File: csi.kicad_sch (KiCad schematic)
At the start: 90 parts, among them J701 WE_68715014522, J702 WE_68715014522, Q701 BSS138W-7-F, Q702 BSS138W-7-F, Q703 BSS138W-7-F, Q704 BSS138W-7-F, U701 PCA9547BS, U702 AP22615, U703 AP22615, U704 NX3DV642, U705 NX3DV642, U706 AP22615, U707 AP22615

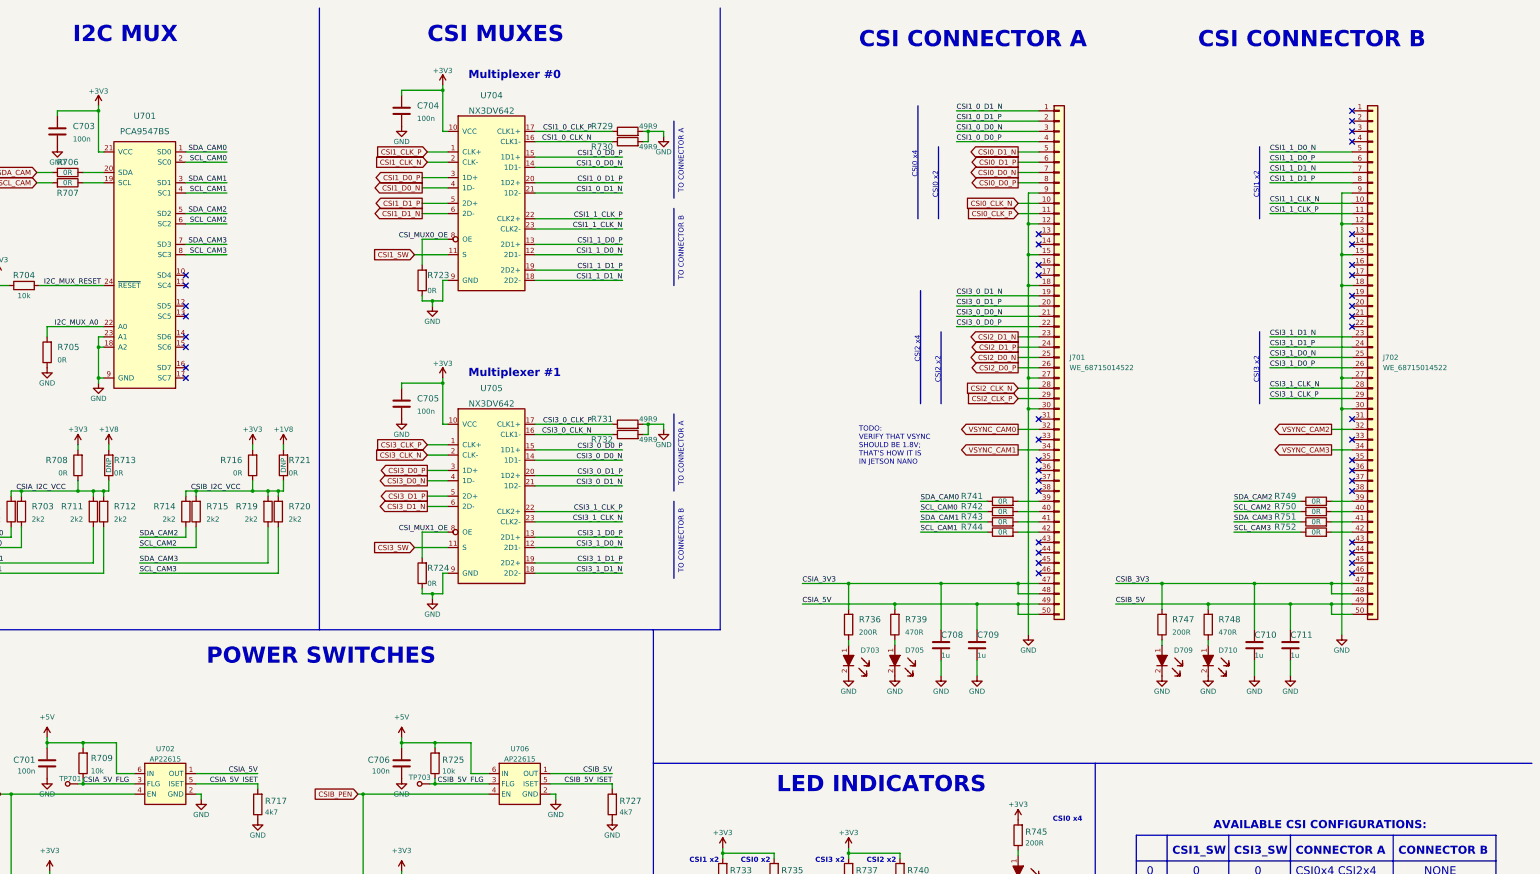
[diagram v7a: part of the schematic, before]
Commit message: Cleaned up schematic after project changes
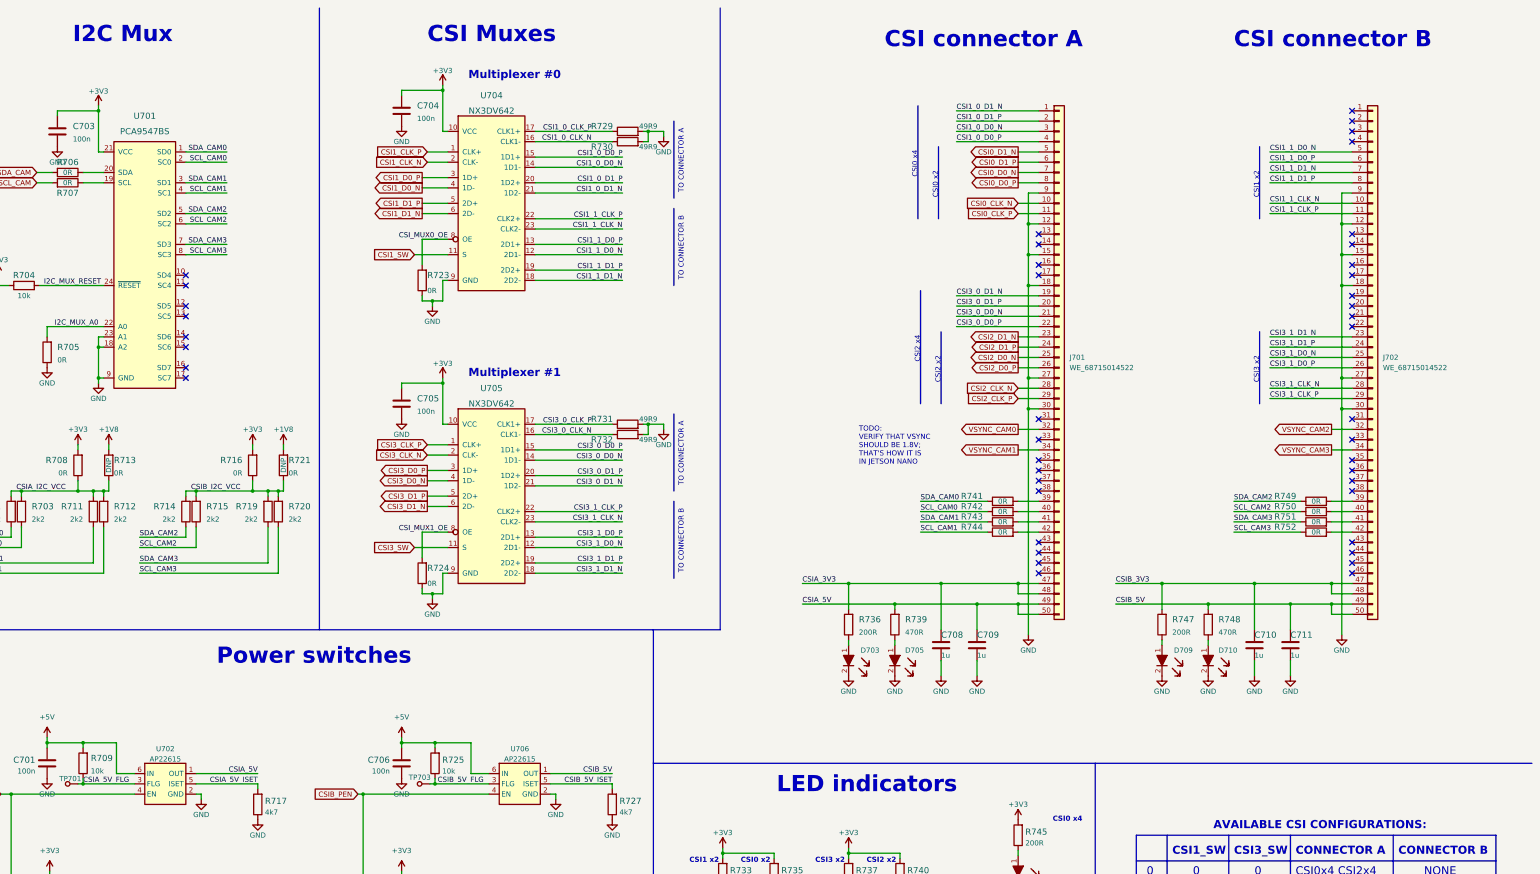
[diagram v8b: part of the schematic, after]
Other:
- note added: "CSI Muxes"
- note added: "CSI connector A"
- note added: "CSI connector B"
- note added: "I2C Mux"
- note added: "LED indicators"
- note added: "Power switches"
- note removed: "CSI CONNECTOR A"
- note removed: "CSI CONNECTOR B"
- note removed: "CSI MUXES"
- note removed: "I2C MUX"
- note removed: "LED INDICATORS"
- note removed: "POWER SWITCHES"
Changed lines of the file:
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@@
     (effects (font (size 1.27 1.27) (thickness 0.254) bold) (justify left bottom))
   )
-  (text "POWER SWITCHES" (at 80.01 175.26 0)
+  (text "Power switches" (at 82.55 175.26 0)
     (effects (font (size 4 4) (thickness 0.8) bold) (justify left bottom))
   )
@@
     (effects (font (size 1.27 1.27)) (justify left bottom))
   )
-  (text "CSI MUXES" (at 134.62 21.59 0)
+  (text "CSI Muxes" (at 134.62 21.59 0)
     (effects (font (size 4 4) (thickness 0.8) bold) (justify left bottom))
   )
@@
     (effects (font (size 2 2) (thickness 0.4) bold) (justify left bottom))
   )
-  (text "CSI CONNECTOR A" (at 241.3 22.86 0)
+  (text "CSI connector A" (at 247.65 22.86 0)
     (effects (font (size 4 4) (thickness 0.8) bold) (justify left bottom))
   )
@@
     (effects (font (size 2 2)) (justify left bottom))
   )
-  (text "LED INDICATORS\n" (at 220.98 207.01 0)
+  (text "LED indicators\n" (at 220.98 207.01 0)
     (effects (font (size 4 4) (thickness 0.8) bold) (justify left bottom))
   )
@@
     (effects (font (size 1.27 1.27)) (justify left bottom))
   )
-  (text "I2C MUX" (at 46.99 21.59 0)
+  (text "I2C Mux" (at 46.99 21.59 0)
     (effects (font (size 4 4) (thickness 0.8) bold) (justify left bottom))
   )
-  (text "CSI CONNECTOR B" (at 325.12 22.86 0)
+  (text "CSI connector B" (at 334.01 22.86 0)
     (effects (font (size 4 4) (thickness 0.8) bold) (justify left bottom))
   )
